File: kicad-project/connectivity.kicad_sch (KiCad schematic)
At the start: 21 parts, among them J5 Conn_01x04, Q1 3LP01M, Q2 PDTC114Y, Q3 Q_NPN_BCE, U4 PAM-7Q-0

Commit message: commit anonimo di thimas
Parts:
- J6: renamed from J?; value Conn_01x08 -> Accelerometer
- Q2: footprint (none) -> Package_TO_SOT_SMD:SOT-23
- Q3: value Q_NPN_BCE -> BC846A; footprint (none) -> Package_TO_SOT_SMD:SOT-23
- Q4, Q5: value ~ -> BC846A; footprint (none) -> Package_TO_SOT_SMD:SOT-23
- gave numbers to parts that had none: 1
- renumbered D5 to D7, J5 to J7
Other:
- note added: "MCU6050"
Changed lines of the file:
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@@
     (stroke (width 0) (type default) (color 0 0 0 0))
+  )
+  (text "MCU6050" (at 204.47 133.35 0)
+    (effects (font (size 1.27 1.27)) (justify left bottom))
   )
   (text "RGB LED" (at 113.03 98.425 180)
@@
   (symbol (lib_id "power:+3V3") (at 29.21 43.18 0) (unit 1)
     (in_bom yes) (on_board yes)
-    (property "Reference" "#PWR054" (id 0) (at 29.21 46.99 0)
+    (property "Reference" "#PWR057" (id 0) (at 29.21 46.99 0)
       (effects (font (size 1.27 1.27)) hide)
     )
@@
   (symbol (lib_id "power:GND") (at 113.03 72.39 0) (unit 1)
     (in_bom yes) (on_board yes)
-    (property "Reference" "#PWR060" (id 0) (at 113.03 78.74 0)
+    (property "Reference" "#PWR063" (id 0) (at 113.03 78.74 0)
       (effects (font (size 1.27 1.27)) hide)
     )
@@
   (symbol (lib_id "power:GND") (at 199.39 101.6 0) (unit 1)
     (in_bom yes) (on_board yes)
-    (property "Reference" "#PWR?" (id 0) (at 199.39 107.95 0)
+    (property "Reference" "#PWR070" (id 0) (at 199.39 107.95 0)
       (effects (font (size 1.27 1.27)) hide)
     )
@@
   (symbol (lib_id "power:GND") (at 104.14 35.56 0) (unit 1)
     (in_bom yes) (on_board yes)
-    (property "Reference" "#PWR058" (id 0) (at 104.14 41.91 0)
+    (property "Reference" "#PWR061" (id 0) (at 104.14 41.91 0)
       (effects (font (size 1.27 1.27)) hide)
     )
@@
   (symbol (lib_id "power:+3V3") (at 49.53 104.14 0) (unit 1)
     (in_bom yes) (on_board yes)
-    (property "Reference" "#PWR055" (id 0) (at 49.53 107.95 0)
+    (property "Reference" "#PWR058" (id 0) (at 49.53 107.95 0)
       (effects (font (size 1.27 1.27)) hide)
     )
@@
   (symbol (lib_id "power:GND") (at 108.585 147.32 0) (unit 1)
     (in_bom yes) (on_board yes)
-    (property "Reference" "#PWR059" (id 0) (at 108.585 153.67 0)
+    (property "Reference" "#PWR062" (id 0) (at 108.585 153.67 0)
       (effects (font (size 1.27 1.27)) hide)
     )
@@
   (symbol (lib_id "Connector_Generic:Conn_01x04") (at 214.63 63.5 0) (unit 1)
     (in_bom yes) (on_board yes) (fields_autoplaced)
-    (property "Reference" "J5" (id 0) (at 217.17 63.4999 0)
+    (property "Reference" "J7" (id 0) (at 217.17 63.4999 0)
       (effects (font (size 1.27 1.27)) (justify left))
     )
@@
       (effects (font (size 1.27 1.27)) (justify left))
     )
-    (property "Value" "~" (id 1) (at 116.205 116.2049 0)
-      (effects (font (size 1.27 1.27)) (justify left))
-    )
-    (property "Footprint" "" (id 2) (at 116.205 112.395 0)
-      (effects (font (size 1.27 1.27)) hide)
-    )
-    (property "Datasheet" "~" (id 3) (at 111.125 114.935 0)
+    (property "Value" "BC846A" (id 1) (at 116.205 116.2049 0)
+      (effects (font (size 1.27 1.27)) (justify left))
+    )
+    (property "Footprint" "Package_TO_SOT_SMD:SOT-23" (id 2) (at 116.205 112.395 0)
+      (effects (font (size 1.27 1.27)) hide)
+    )
+    (property "Datasheet" "https://www.mouser.it/datasheet/2/308/1/BC846ALT1_D-2310268.pdf" (id 3) (at 111.125 114.935 0)
       (effects (font (size 1.27 1.27)) hide)
     )
@@
   (symbol (lib_id "power:GND") (at 199.39 138.43 0) (unit 1)
     (in_bom yes) (on_board yes)
-    (property "Reference" "#PWR?" (id 0) (at 199.39 144.78 0)
+    (property "Reference" "#PWR073" (id 0) (at 199.39 144.78 0)
       (effects (font (size 1.27 1.27)) hide)
     )
@@
   (symbol (lib_id "power:+3V3") (at 205.74 62.23 0) (unit 1)
     (in_bom yes) (on_board yes)
-    (property "Reference" "#PWR067" (id 0) (at 205.74 66.04 0)
+    (property "Reference" "#PWR075" (id 0) (at 205.74 66.04 0)
       (effects (font (size 1.27 1.27)) hide)
     )
@@
   (symbol (lib_id "power:GND") (at 113.665 147.32 0) (unit 1)
     (in_bom yes) (on_board yes)
-    (property "Reference" "#PWR062" (id 0) (at 113.665 153.67 0)
+    (property "Reference" "#PWR065" (id 0) (at 113.665 153.67 0)
       (effects (font (size 1.27 1.27)) hide)
     )
@@
   (symbol (lib_id "power:+12V") (at 128.27 108.585 0) (unit 1)
     (in_bom yes) (on_board yes)
-    (property "Reference" "#PWR065" (id 0) (at 128.27 112.395 0)
+    (property "Reference" "#PWR068" (id 0) (at 128.27 112.395 0)
       (effects (font (size 1.27 1.27)) hide)
     )
@@
   (symbol (lib_id "power:+3V3") (at 199.39 123.19 0) (unit 1)
     (in_bom yes) (on_board yes)
-    (property "Reference" "#PWR?" (id 0) (at 199.39 127 0)
+    (property "Reference" "#PWR071" (id 0) (at 199.39 127 0)
       (effects (font (size 1.27 1.27)) hide)
     )
@@
   (symbol (lib_id "power:+12V") (at 99.06 108.585 0) (unit 1)
     (in_bom yes) (on_board yes)
-    (property "Reference" "#PWR057" (id 0) (at 99.06 112.395 0)
+    (property "Reference" "#PWR060" (id 0) (at 99.06 112.395 0)
       (effects (font (size 1.27 1.27)) hide)
     )
@@
   (symbol (lib_id "power:+12V") (at 113.665 108.585 0) (unit 1)
     (in_bom yes) (on_board yes)
-    (property "Reference" "#PWR061" (id 0) (at 113.665 112.395 0)
+    (property "Reference" "#PWR064" (id 0) (at 113.665 112.395 0)
       (effects (font (size 1.27 1.27)) hide)
     )
@@
   (symbol (lib_id "power:+3V3") (at 199.39 99.06 0) (unit 1)
     (in_bom yes) (on_board yes)
-    (property "Reference" "#PWR?" (id 0) (at 199.39 102.87 0)
+    (property "Reference" "#PWR069" (id 0) (at 199.39 102.87 0)
       (effects (font (size 1.27 1.27)) hide)
     )
@@
   (symbol (lib_id "power:GND") (at 118.745 147.32 0) (unit 1)
     (in_bom yes) (on_board yes)
-    (property "Reference" "#PWR063" (id 0) (at 118.745 153.67 0)
+    (property "Reference" "#PWR066" (id 0) (at 118.745 153.67 0)
       (effects (font (size 1.27 1.27)) hide)
     )
@@
   (symbol (lib_id "power:GND") (at 200.66 58.42 0) (unit 1)
     (in_bom yes) (on_board yes)
-    (property "Reference" "#PWR066" (id 0) (at 200.66 64.77 0)
+    (property "Reference" "#PWR074" (id 0) (at 200.66 64.77 0)
       (effects (font (size 1.27 1.27)) hide)
     )
@@
   (symbol (lib_id "power:GND") (at 127 35.56 0) (unit 1)
     (in_bom yes) (on_board yes)
-    (property "Reference" "#PWR064" (id 0) (at 127 41.91 0)
+    (property "Reference" "#PWR067" (id 0) (at 127 41.91 0)
       (effects (font (size 1.27 1.27)) hide)
     )
@@
   (symbol (lib_id "Connector_Generic:Conn_01x05") (at 185.42 104.14 0) (mirror y) (unit 1)
     (in_bom yes) (on_board yes) (fields_autoplaced)
-    (property "Reference" "J?" (id 0) (at 185.42 92.71 0))
+    (property "Reference" "J5" (id 0) (at 185.42 92.71 0))
     (property "Value" "Compass" (id 1) (at 185.42 95.25 0))
     (property "Footprint" "" (id 2) (at 185.42 104.14 0)
@@
   (symbol (lib_id "Connector_Generic:Conn_01x08") (at 185.42 130.81 0) (mirror y) (unit 1)
     (in_bom yes) (on_board yes) (fields_autoplaced)
-    (property "Reference" "J?" (id 0) (at 185.42 116.84 0))
-    (property "Value" "Conn_01x08" (id 1) (at 185.42 119.38 0))
+    (property "Reference" "J6" (id 0) (at 185.42 116.84 0))
+    (property "Value" "Accelerometer" (id 1) (at 185.42 119.38 0))
     (property "Footprint" "" (id 2) (at 185.42 130.81 0)
       (effects (font (size 1.27 1.27)) hide)
@@
   (symbol (lib_id "power:GND") (at 49.53 133.35 0) (unit 1)
     (in_bom yes) (on_board yes)
-    (property "Reference" "#PWR056" (id 0) (at 49.53 139.7 0)
+    (property "Reference" "#PWR059" (id 0) (at 49.53 139.7 0)
       (effects (font (size 1.27 1.27)) hide)
     )
@@
       (effects (font (size 1.27 1.27)) (justify left))
     )
-    (property "Value" "Q_NPN_BCE" (id 1) (at 100.33 120.015 0)
-      (effects (font (size 1.27 1.27)) (justify left))
-    )
-    (property "Footprint" "" (id 2) (at 101.6 112.395 0)
-      (effects (font (size 1.27 1.27)) hide)
-    )
-    (property "Datasheet" "~" (id 3) (at 96.52 114.935 0)
+    (property "Value" "BC846A" (id 1) (at 100.33 120.015 0)
+      (effects (font (size 1.27 1.27)) (justify left))
+    )
+    (property "Footprint" "Package_TO_SOT_SMD:SOT-23" (id 2) (at 101.6 112.395 0)
+      (effects (font (size 1.27 1.27)) hide)
+    )
+    (property "Datasheet" "https://www.mouser.it/datasheet/2/308/1/BC846ALT1_D-2310268.pdf" (id 3) (at 96.52 114.935 0)
       (effects (font (size 1.27 1.27)) hide)
     )
@@
       (effects (font (size 1.27 1.27)) (justify left))
     )
-    (property "Value" "~" (id 1) (at 130.81 116.2049 0)
-      (effects (font (size 1.27 1.27)) (justify left))
-    )
-    (property "Footprint" "" (id 2) (at 130.81 112.395 0)
-      (effects (font (size 1.27 1.27)) hide)
-    )
-    (property "Datasheet" "~" (id 3) (at 125.73 114.935 0)
+    (property "Value" "BC846A" (id 1) (at 130.81 116.2049 0)
+      (effects (font (size 1.27 1.27)) (justify left))
+    )
+    (property "Footprint" "Package_TO_SOT_SMD:SOT-23" (id 2) (at 130.81 112.395 0)
+      (effects (font (size 1.27 1.27)) hide)
+    )
+    (property "Datasheet" "https://www.mouser.it/datasheet/2/308/1/BC846ALT1_D-2310268.pdf" (id 3) (at 125.73 114.935 0)
       (effects (font (size 1.27 1.27)) hide)
     )
@@
   (symbol (lib_id "power:GND") (at 199.39 125.73 0) (unit 1)
     (in_bom yes) (on_board yes)
-    (property "Reference" "#PWR?" (id 0) (at 199.39 132.08 0)
+    (property "Reference" "#PWR072" (id 0) (at 199.39 132.08 0)
       (effects (font (size 1.27 1.27)) hide)
     )
@@
   (symbol (lib_id "Device:LED_RGB") (at 113.665 142.24 90) (unit 1)
     (in_bom yes) (on_board yes)
-    (property "Reference" "D5" (id 0) (at 122.047 141.0716 90)
+    (property "Reference" "D7" (id 0) (at 122.047 141.0716 90)
       (effects (font (size 1.27 1.27)) (justify right))
     )
@@
       (effects (font (size 1.27 1.27)) (justify left))
     )
-    (property "Footprint" "" (id 2) (at 46.99 124.46 0)
-      (effects (font (size 1.27 1.27)) (justify left) hide)
-    )
+    (property "Footprint" "Package_TO_SOT_SMD:SOT-23" (id 2) (at 46.99 124.46 0)
+      (effects (font (size 1.27 1.27)) (justify left) hide)
+    )

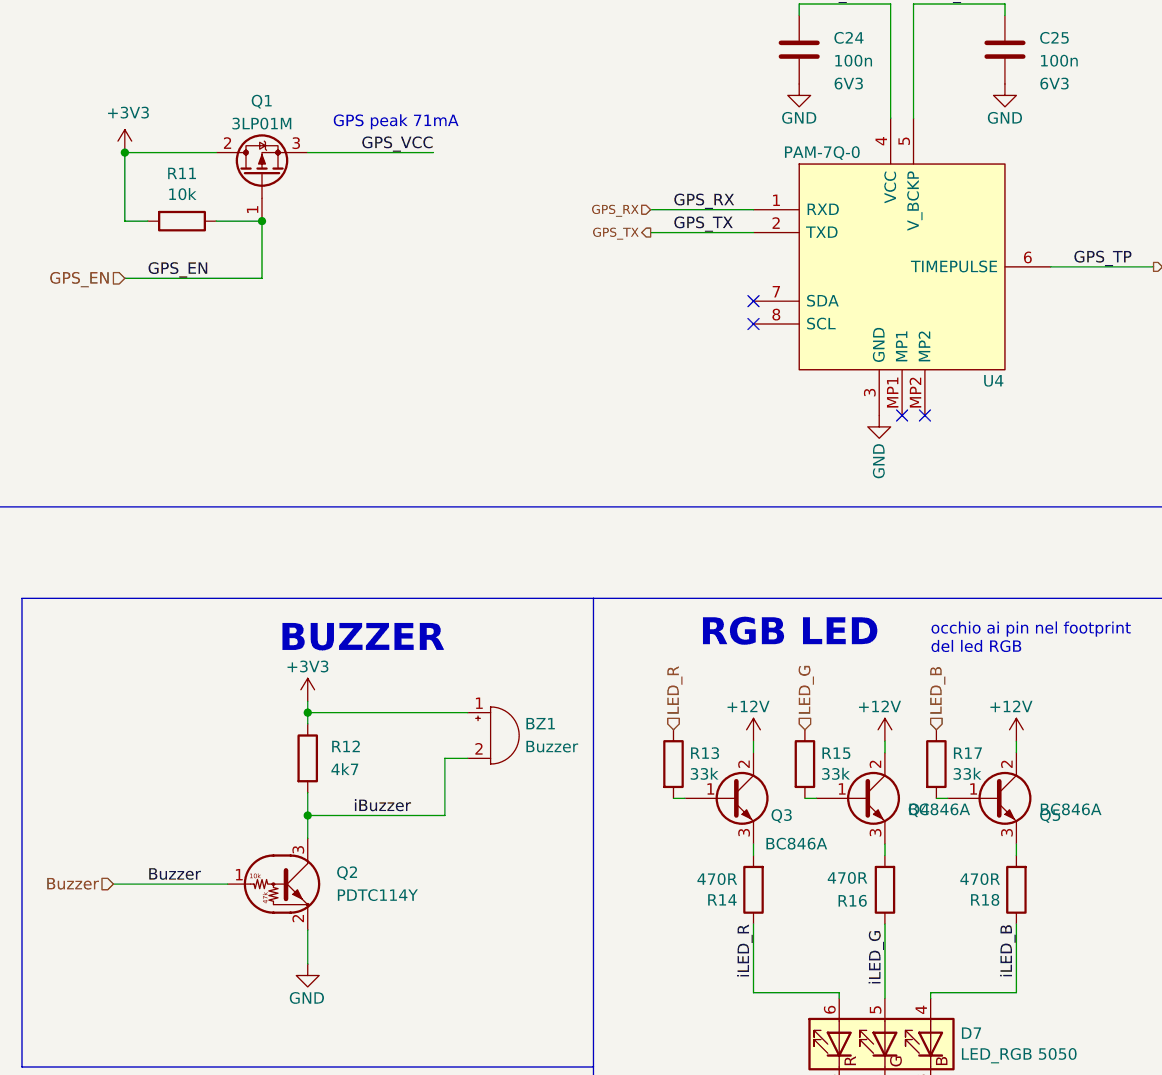
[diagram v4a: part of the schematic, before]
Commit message: hw: add mounting holes
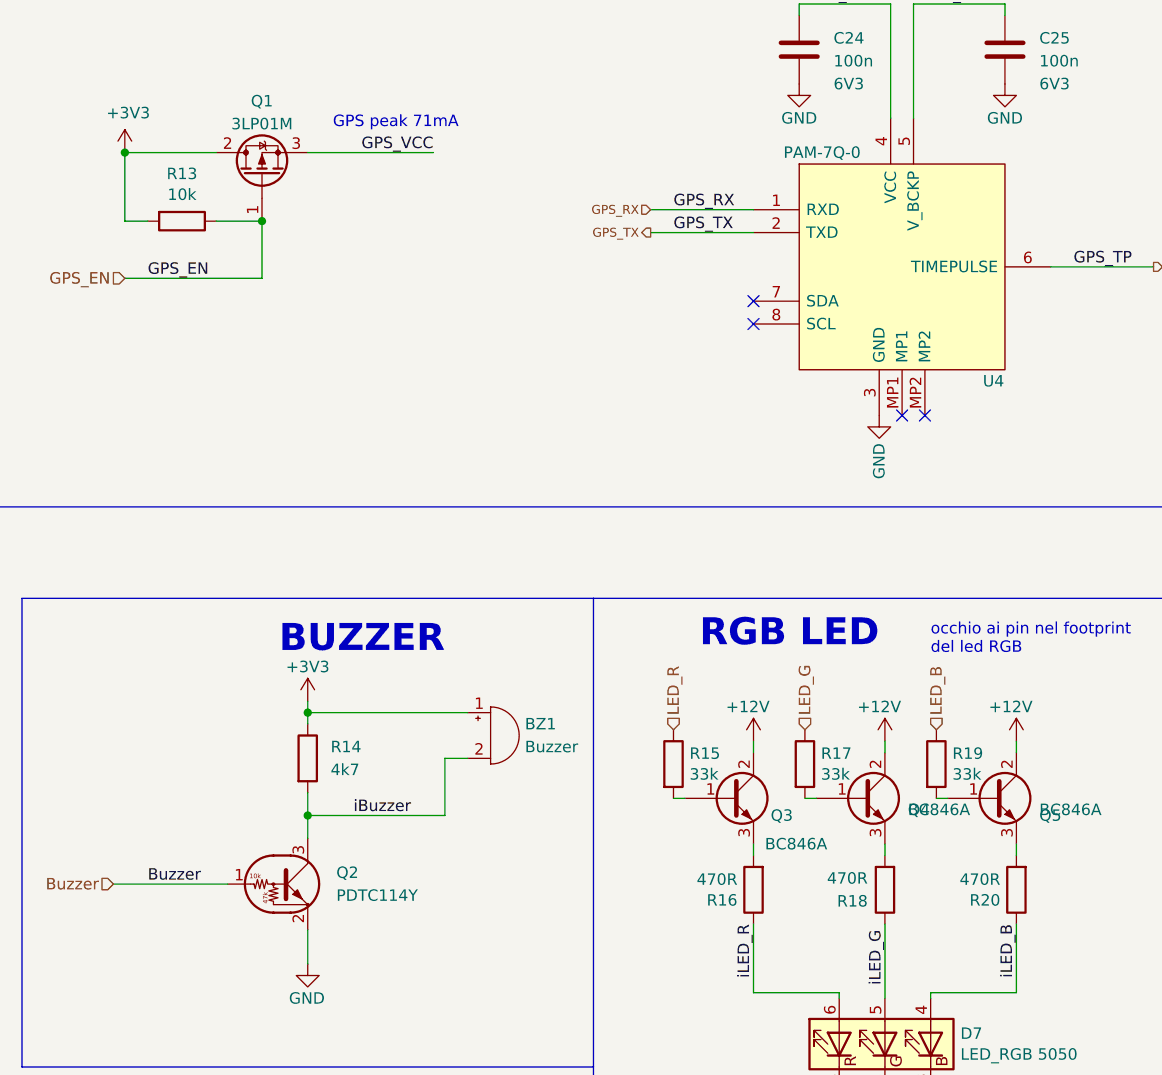
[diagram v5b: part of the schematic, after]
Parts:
- renumbered R11 to R13, R12 to R14, R13 to R15, R14 to R16, R15 to R17, R16 to R18, R17 to R19, R18 to R20
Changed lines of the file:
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@@
   (symbol (lib_id "Device:R") (at 35.56 50.8 270) (unit 1)
     (in_bom yes) (on_board yes)
-    (property "Reference" "R11" (id 0) (at 35.56 45.5422 90))
+    (property "Reference" "R13" (id 0) (at 35.56 45.5422 90))
     (property "Value" "10k" (id 1) (at 35.56 47.8536 90))
     (property "Footprint" "Resistor_SMD:R_0603_1608Metric" (id 2) (at 35.56 49.022 90)
@@
   (symbol (lib_id "Device:R") (at 99.06 125.095 180) (unit 1)
     (in_bom yes) (on_board yes)
-    (property "Reference" "R14" (id 0) (at 97.282 126.2634 0)
+    (property "Reference" "R16" (id 0) (at 97.282 126.2634 0)
       (effects (font (size 1.27 1.27)) (justify left))
     )
@@
   (symbol (lib_id "Device:R") (at 104.775 111.125 0) (unit 1)
     (in_bom yes) (on_board yes)
-    (property "Reference" "R15" (id 0) (at 106.553 109.9566 0)
+    (property "Reference" "R17" (id 0) (at 106.553 109.9566 0)
       (effects (font (size 1.27 1.27)) (justify left))
     )
@@
   (symbol (lib_id "Device:R") (at 90.17 111.125 0) (unit 1)
     (in_bom yes) (on_board yes)
-    (property "Reference" "R13" (id 0) (at 91.948 109.9566 0)
+    (property "Reference" "R15" (id 0) (at 91.948 109.9566 0)
       (effects (font (size 1.27 1.27)) (justify left))
     )
@@
   (symbol (lib_id "Device:R") (at 119.38 111.125 0) (unit 1)
     (in_bom yes) (on_board yes)
-    (property "Reference" "R17" (id 0) (at 121.158 109.9566 0)
+    (property "Reference" "R19" (id 0) (at 121.158 109.9566 0)
       (effects (font (size 1.27 1.27)) (justify left))
     )
@@
   (symbol (lib_id "Device:R") (at 113.665 125.095 180) (unit 1)
     (in_bom yes) (on_board yes)
-    (property "Reference" "R16" (id 0) (at 111.76 126.365 0)
+    (property "Reference" "R18" (id 0) (at 111.76 126.365 0)
       (effects (font (size 1.27 1.27)) (justify left))
     )
@@
   (symbol (lib_id "Device:R") (at 49.53 110.49 0) (unit 1)
     (in_bom yes) (on_board yes) (fields_autoplaced)
-    (property "Reference" "R12" (id 0) (at 52.07 109.2199 0)
+    (property "Reference" "R14" (id 0) (at 52.07 109.2199 0)
       (effects (font (size 1.27 1.27)) (justify left))
     )
@@
   (symbol (lib_id "Device:R") (at 128.27 125.095 180) (unit 1)
     (in_bom yes) (on_board yes)
-    (property "Reference" "R18" (id 0) (at 126.492 126.2634 0)
-      (effects (font (size 1.27 1.27)) (justify left))
-    )
+    (property "Reference" "R20" (id 0) (at 126.492 126.2634 0)
+      (effects (font (size 1.27 1.27)) (justify left))
+    )

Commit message: hw: add last footprints
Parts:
- J5: footprint (none) -> Connector_PinHeader_2.54mm:PinHeader_1x05_P2.54mm_Vertical
- J6: footprint (none) -> Connector_PinHeader_2.54mm:PinHeader_1x08_P2.54mm_Vertical
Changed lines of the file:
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@@
     (property "Reference" "J5" (id 0) (at 185.42 92.71 0))
     (property "Value" "Compass" (id 1) (at 185.42 95.25 0))
-    (property "Footprint" "" (id 2) (at 185.42 104.14 0)
+    (property "Footprint" "Connector_PinHeader_2.54mm:PinHeader_1x05_P2.54mm_Vertical" (id 2) (at 185.42 104.14 0)
       (effects (font (size 1.27 1.27)) hide)
     )
@@
     (property "Reference" "J6" (id 0) (at 185.42 116.84 0))
     (property "Value" "Accelerometer" (id 1) (at 185.42 119.38 0))
-    (property "Footprint" "" (id 2) (at 185.42 130.81 0)
+    (property "Footprint" "Connector_PinHeader_2.54mm:PinHeader_1x08_P2.54mm_Vertical" (id 2) (at 185.42 130.81 0)
       (effects (font (size 1.27 1.27)) hide)
     )

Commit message: hw: first layout draft
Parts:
- removed D7: LED_RGB 5050, LED_SMD:LED_RGB_1210, symbol Device:LED_RGB
- added D7: LED_RGB 5050, LED_SMD:LED_RGB_1210, symbol Device:LED_RGBK
- J7: value Conn_01x04 -> OLED; footprint Connector_PinHeader_2.54mm:PinHeader_1x04_P2.54mm_Vertical_SMD_Pin1Left -> Connector_PinHeader_2.54mm:PinHeader_1x04_P2.54mm_Vertical
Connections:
- net I2C1_SCL is gone; now on net SCL: J7.3 (Pin_3)
- net I2C1_SDA is gone; now on net SDA: J7.4 (Pin_4)
- net GND: now also D7.4 (K)
- net iLED_B: now also D7.3 (BA)
- net iLED_G: now also D7.2 (GA)
- net iLED_R: now also D7.1 (RA)
- net DRDY renamed CMP_DRDY
- net INT renamed ACC_INT
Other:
- moved on the sheet: J5, J6

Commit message: hw: power routing
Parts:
- J5: footprint Connector_PinHeader_2.54mm:PinHeader_1x05_P2.54mm_Vertical -> Connector_PinHeader_2.54mm:PinHeader_1x05_P2.54mm_Horizontal
- J6: footprint Connector_PinHeader_2.54mm:PinHeader_1x08_P2.54mm_Vertical -> Connector_PinHeader_2.54mm:PinHeader_1x08_P2.54mm_Horizontal
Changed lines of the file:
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@@
     (property "Reference" "J5" (id 0) (at 196.85 92.71 0))
     (property "Value" "Compass" (id 1) (at 196.85 95.25 0))
-    (property "Footprint" "Connector_PinHeader_2.54mm:PinHeader_1x05_P2.54mm_Vertical" (id 2) (at 196.85 104.14 0)
+    (property "Footprint" "Connector_PinHeader_2.54mm:PinHeader_1x05_P2.54mm_Horizontal" (id 2) (at 196.85 104.14 0)
       (effects (font (size 1.27 1.27)) hide)
     )
@@
     (property "Reference" "J6" (id 0) (at 196.85 116.84 0))
     (property "Value" "Accelerometer" (id 1) (at 196.85 119.38 0))
-    (property "Footprint" "Connector_PinHeader_2.54mm:PinHeader_1x08_P2.54mm_Vertical" (id 2) (at 196.85 130.81 0)
+    (property "Footprint" "Connector_PinHeader_2.54mm:PinHeader_1x08_P2.54mm_Horizontal" (id 2) (at 196.85 130.81 0)
       (effects (font (size 1.27 1.27)) hide)
     )
